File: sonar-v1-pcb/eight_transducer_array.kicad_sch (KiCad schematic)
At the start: 22 parts, among them U201 ADS8568SPM

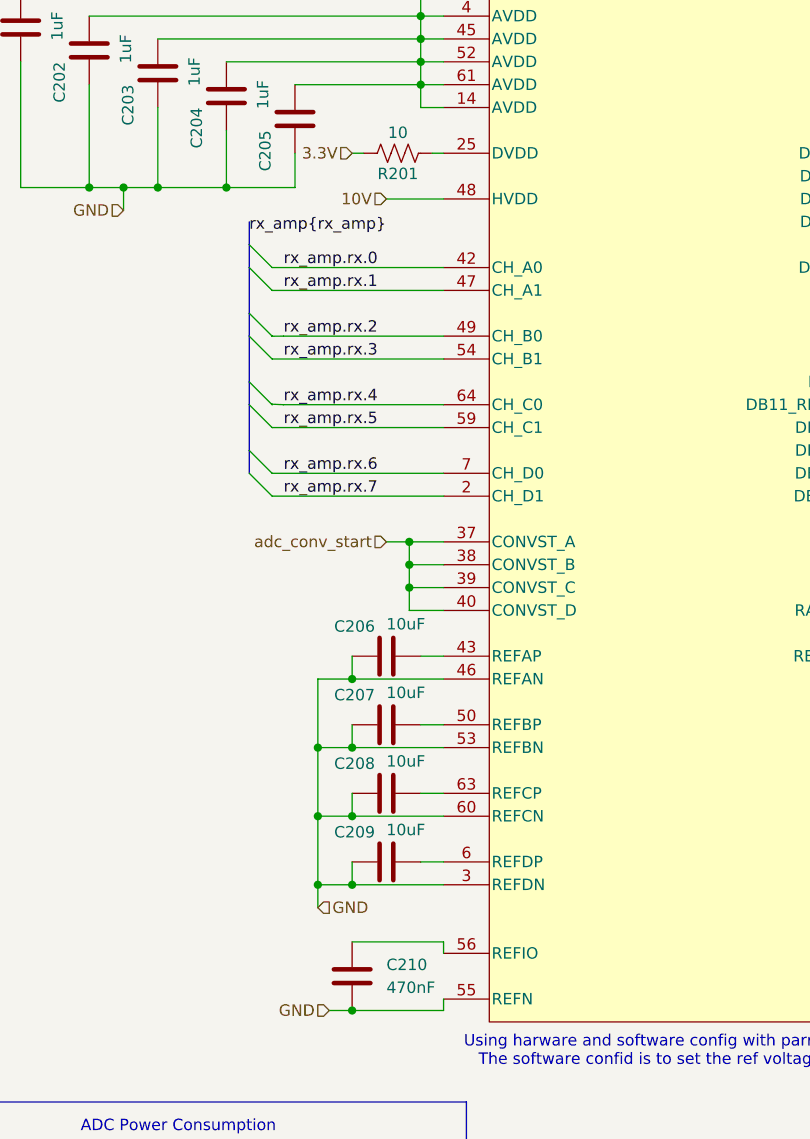
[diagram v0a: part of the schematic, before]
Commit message: Fix pinout
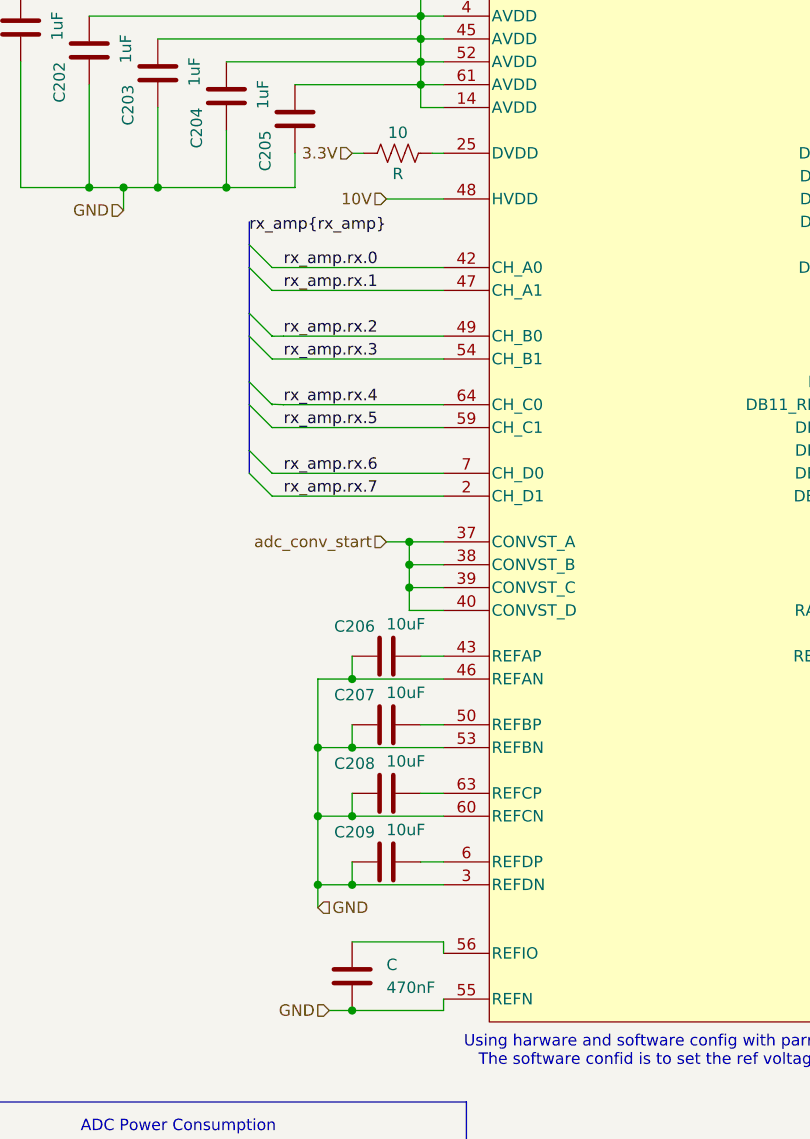
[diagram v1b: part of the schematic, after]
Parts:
- renumbered C210 to C, R201 to R

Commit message: Fix the annoattion thing
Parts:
- renumbered C to C210, R to R201
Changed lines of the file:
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@@
 		(on_board yes)
 		(dnp no)
-		(property "Reference" "R"
+		(property "Reference" "R201"
 			(at 133.35 54.356 90)
 			(effects
@@
 			(project "sonar"
 				(path "/f72ceae0-eee4-4385-b0e8-639846bcb5f2/293969c4-9575-41aa-bb6a-e94ffb52e407"
-					(reference "R1702")
+					(reference "R1701")
 					(unit 1)
 				)
 				(path "/f72ceae0-eee4-4385-b0e8-639846bcb5f2/d3b8d639-c387-46bd-9010-317ff5495a13"
 					(reference "R401")
+					(unit 1)
+				)
+				(path "/f72ceae0-eee4-4385-b0e8-639846bcb5f2/d78844ef-eb5d-4b24-a5c3-8824db20c2bc"
+					(reference "R201")
 					(unit 1)
 				)
@@
 			(project "sonar"
 				(path "/f72ceae0-eee4-4385-b0e8-639846bcb5f2/293969c4-9575-41aa-bb6a-e94ffb52e407"
-					(reference "C1712")
+					(reference "C1711")
 					(unit 1)
 				)
@@
 			(project "sonar"
 				(path "/f72ceae0-eee4-4385-b0e8-639846bcb5f2/293969c4-9575-41aa-bb6a-e94ffb52e407"
-					(reference "R1705")
+					(reference "R1704")
 					(unit 1)
 				)
@@
 			(project "sonar"
 				(path "/f72ceae0-eee4-4385-b0e8-639846bcb5f2/293969c4-9575-41aa-bb6a-e94ffb52e407"
-					(reference "R1706")
+					(reference "R1705")
 					(unit 1)
 				)
@@
 			(project "sonar"
 				(path "/f72ceae0-eee4-4385-b0e8-639846bcb5f2/293969c4-9575-41aa-bb6a-e94ffb52e407"
-					(reference "R1703")
+					(reference "R1702")
 					(unit 1)
 				)
@@
 			(project "sonar"
 				(path "/f72ceae0-eee4-4385-b0e8-639846bcb5f2/293969c4-9575-41aa-bb6a-e94ffb52e407"
-					(reference "R1704")
+					(reference "R1703")
 					(unit 1)
 				)
@@
 			(project "sonar"
 				(path "/f72ceae0-eee4-4385-b0e8-639846bcb5f2/293969c4-9575-41aa-bb6a-e94ffb52e407"
-					(reference "C1713")
+					(reference "C1712")
 					(unit 1)
 				)
@@
 		(dnp no)
 		(fields_autoplaced yes)
-		(property "Reference" "C"
+		(property "Reference" "C210"
 			(at 132.08 142.2399 0)
 			(effects
@@
 			(project "sonar"
 				(path "/f72ceae0-eee4-4385-b0e8-639846bcb5f2/293969c4-9575-41aa-bb6a-e94ffb52e407"
-					(reference "C1711")
+					(reference "C1710")
 					(unit 1)
 				)
 				(path "/f72ceae0-eee4-4385-b0e8-639846bcb5f2/d3b8d639-c387-46bd-9010-317ff5495a13"
 					(reference "C410")
+					(unit 1)
+				)
+				(path "/f72ceae0-eee4-4385-b0e8-639846bcb5f2/d78844ef-eb5d-4b24-a5c3-8824db20c2bc"
+					(reference "C210")
 					(unit 1)
 				)
@@
 			(project "sonar"
 				(path "/f72ceae0-eee4-4385-b0e8-639846bcb5f2/293969c4-9575-41aa-bb6a-e94ffb52e407"
-					(reference "C1714")
+					(reference "C1713")
 					(unit 1)
 				)
@@
 			(project "sonar"
 				(path "/f72ceae0-eee4-4385-b0e8-639846bcb5f2/293969c4-9575-41aa-bb6a-e94ffb52e407"
-					(reference "C1717")
+					(reference "C1716")
 					(unit 1)
 				)
@@
 			(project "sonar"
 				(path "/f72ceae0-eee4-4385-b0e8-639846bcb5f2/293969c4-9575-41aa-bb6a-e94ffb52e407"
-					(reference "C1715")
+					(reference "C1714")
 					(unit 1)
 				)
@@
 			(project "sonar"
 				(path "/f72ceae0-eee4-4385-b0e8-639846bcb5f2/293969c4-9575-41aa-bb6a-e94ffb52e407"
-					(reference "C1716")
-					(unit 1)
-				)
+					(reference "C1715")
+					(unit 1)
+				)
